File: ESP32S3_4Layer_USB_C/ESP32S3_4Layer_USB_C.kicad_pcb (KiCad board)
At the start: 4 copper layers, 48.2 x 59.8 mm, 38 parts, among them J1 Conn_01x04_Pin, J2 Conn_01x10_Socket, J3 Conn_01x10_Socket, P1 USB_C_Plug_USB2.0, SW1 SW_Push, SW2 SW_Push, U1 MP1584EN-LF-Z, U2 ESP32-WROOM-32, U3 CP2102N-Axx-xQFN24

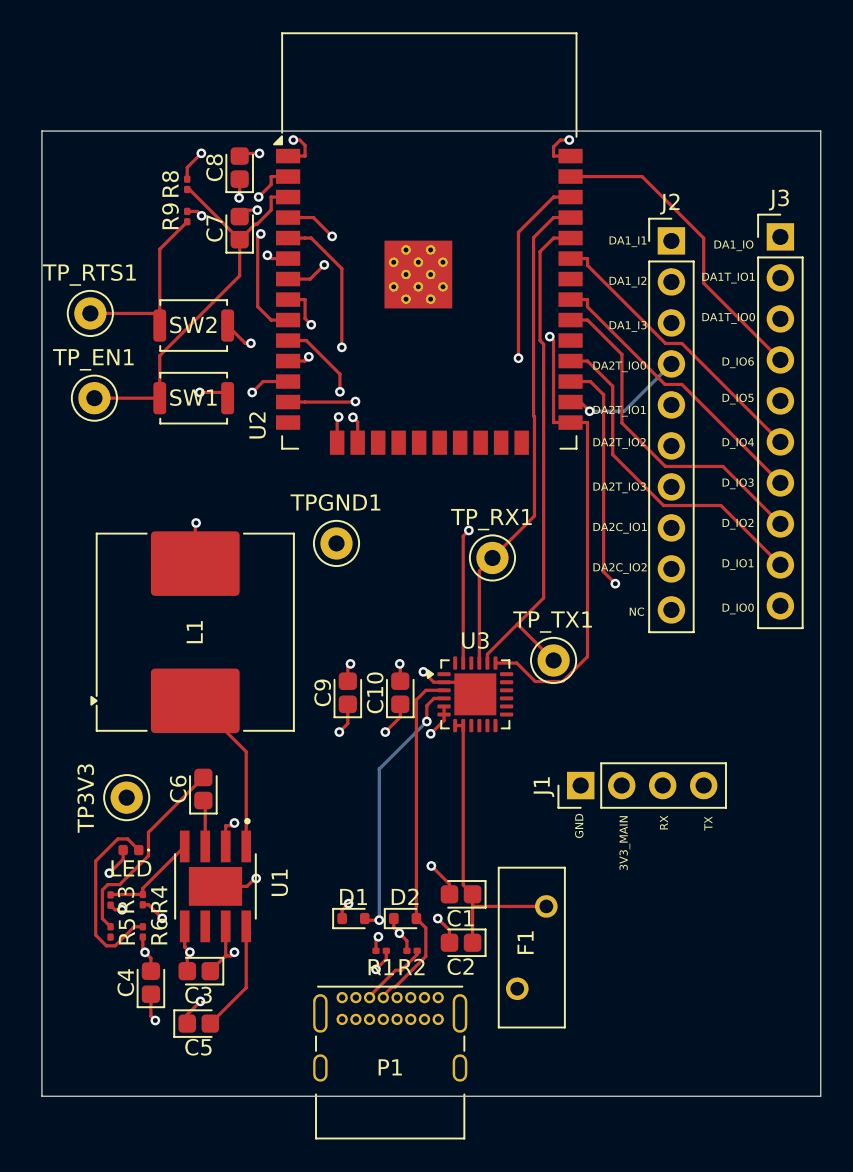
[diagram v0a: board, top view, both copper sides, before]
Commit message: Fixed some errors from routing traces
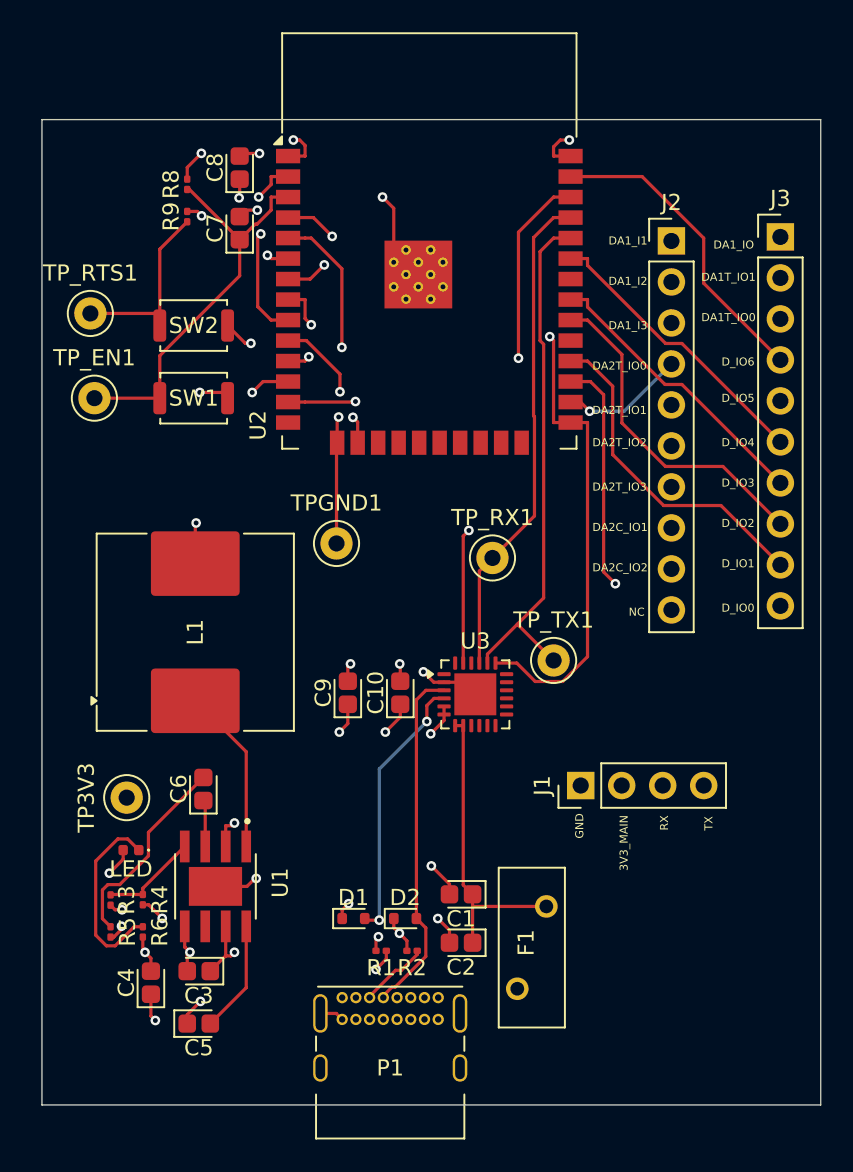
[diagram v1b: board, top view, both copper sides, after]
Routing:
- net GND: track 41.9 -> 54.3 mm, vias 19 -> 21
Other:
- board size 48.2 x 59.8 mm -> 48.2 x 61 mm
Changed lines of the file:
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@@
 	)
 	(gr_rect
-		(start 129.15 68.66)
-		(end 177.4 128.46)
+		(start 129.15 67.95)
+		(end 177.4 129)
 		(stroke
 			(width 0.05)
@@
 	)
 	(segment
+		(start 146.4 123.33)
+		(end 147.38 123.33)
+		(width 0.2)
+		(layer "F.Cu")
+		(net 1)
+	)
+	(segment
 		(start 144.4 70.21)
 		(end 145.4517 70.21)
@@
 	)
 	(segment
+		(start 133.599999 118.6)
+		(end 134.079998 118.120001)
+		(width 0.2)
+		(layer "F.Cu")
+		(net 1)
+	)
+	(segment
 		(start 142.425 114.965)
 		(end 142.3467 114.965)
@@
 	)
 	(segment
+		(start 134.079998 118.120001)
+		(end 134.079998 117.923158)
+		(width 0.2)
+		(layer "F.Cu")
+		(net 1)
+	)
+	(segment
 		(start 161.9 70.21)
 		(end 160.8483 70.21)
@@
 	)
 	(segment
+		(start 147.4 88.01)
+		(end 147.44 87.97)
+		(width 0.2)
+		(layer "F.Cu")
+		(net 1)
+	)
+	(segment
 		(start 154.0625 102.81)
 		(end 155.25 102.81)
@@
 	)
 	(segment
+		(start 147.4 94.21)
+		(end 147.4 88.01)
+		(width 0.2)
+		(layer "F.Cu")
+		(net 1)
+	)
+	(segment
 		(start 141.5622 70.0478)
 		(end 141.4 70.21)
@@
 	)
 	(segment
+		(start 150.945 76.025)
+		(end 150.945 73.445)
+		(width 0.2)
+		(layer "F.Cu")
+		(net 1)
+	)
+	(segment
+		(start 147.38 123.33)
+		(end 147.75 123.7)
+		(width 0.2)
+		(layer "F.Cu")
+		(net 1)
+	)
+	(segment
 		(start 153.6753 117.45)
 		(end 154.4 118.1747)
@@
 	)
 	(segment
+		(start 133.4 118.6)
+		(end 133.599999 118.6)
+		(width 0.2)
+		(layer "F.Cu")
+		(net 1)
+	)
+	(segment
 		(start 135.4 118.6)
 		(end 135.4 119.4088)
@@
 		(net 1)
 	)
+	(segment
+		(start 150.945 73.445)
+		(end 150.25 72.75)
+		(width 0.2)
+		(layer "F.Cu")
+		(net 1)
+	)
 	(via
 		(at 148.267 101.6732)
@@
 	)
 	(via
+		(at 134.079998 117.923158)
+		(size 0.6)
+		(drill 0.3)
+		(layers "F.Cu" "B.Cu")
+		(net 1)
+	)
+	(via
 		(at 152.7829 102.1661)
 		(size 0.6)
@@
 		(size 0.6)
 		(drill 0.3)
+		(layers "F.Cu" "B.Cu")
+		(net 1)
+	)
+	(via
+		(at 150.25 72.75)
+		(size 0.6)
+		(drill 0.3)
